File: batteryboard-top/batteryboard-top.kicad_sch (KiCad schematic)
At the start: 6 parts

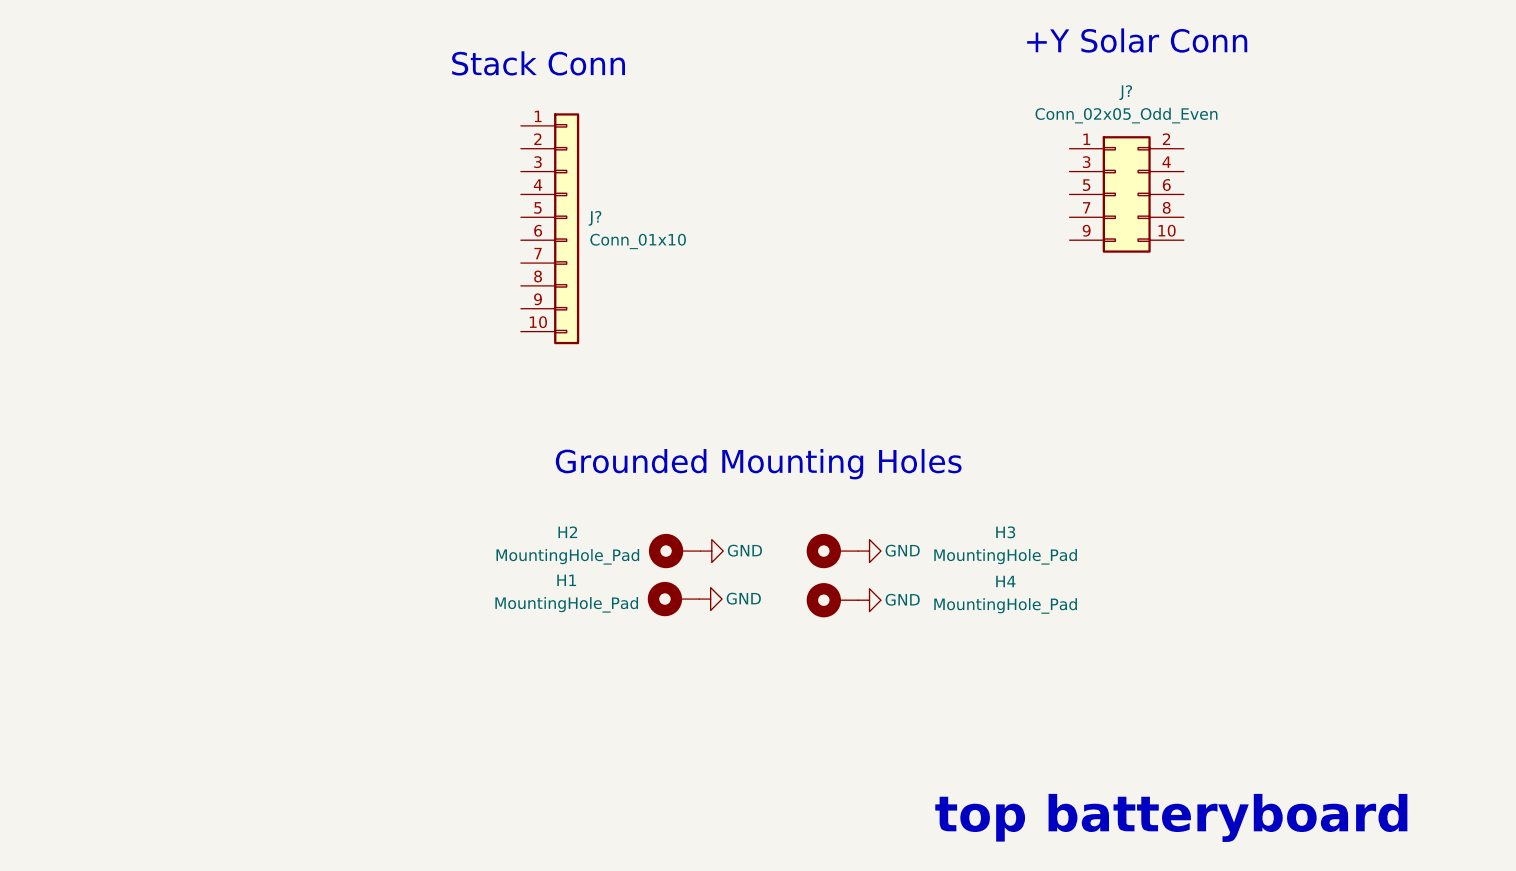
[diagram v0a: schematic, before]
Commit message: labeled connections
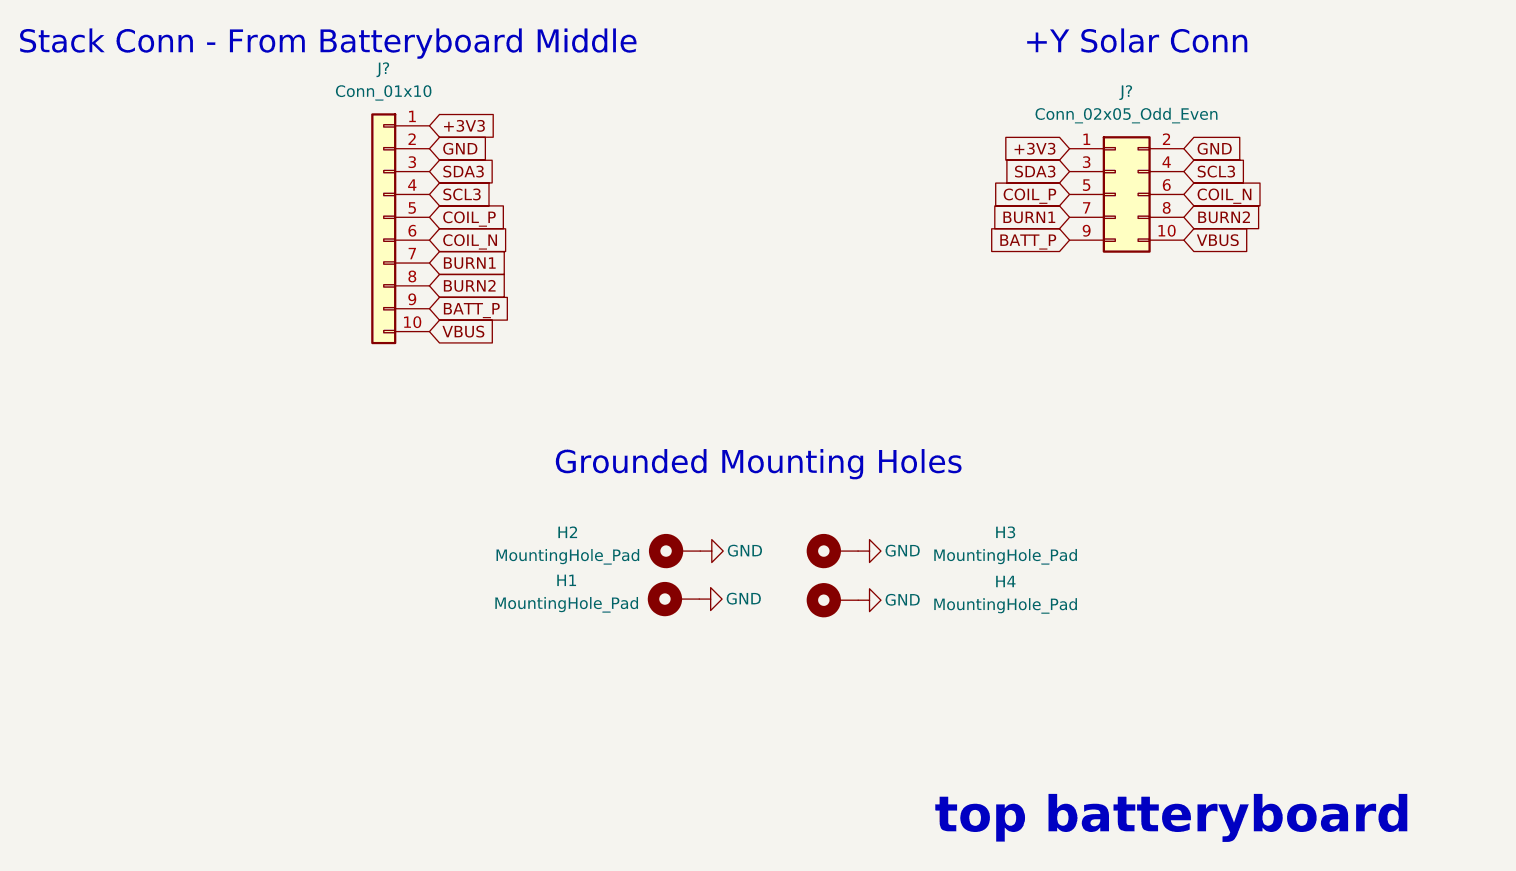
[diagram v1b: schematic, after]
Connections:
- net GND: now also J?.2 (Pin_2), J?.2 (Pin_2)
- net +3V3: now reaches J?.1 (Pin_1)
- net +3V3: now also J?.1 (Pin_1)
- net VBUS: now reaches J?.10 (Pin_10)
- net VBUS: now also J?.10 (Pin_10)
- net SDA3: now reaches J?.3 (Pin_3)
- net SDA3: now also J?.3 (Pin_3)
- net SCL3: now reaches J?.4 (Pin_4)
- net SCL3: now also J?.4 (Pin_4)
- net COIL_P: now reaches J?.5 (Pin_5)
- net COIL_P: now also J?.5 (Pin_5)
- net COIL_N: now reaches J?.6 (Pin_6)
- net COIL_N: now also J?.6 (Pin_6)
- net BURN1: now reaches J?.7 (Pin_7)
- net BURN1: now also J?.7 (Pin_7)
- net BURN2: now reaches J?.8 (Pin_8)
- net BURN2: now also J?.8 (Pin_8)
- net BATT_P: now reaches J?.9 (Pin_9)
- net BATT_P: now also J?.9 (Pin_9)
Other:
- note added: "Stack Conn - From Batteryboard Middle"
- note removed: "Stack Conn"
- moved on the sheet: J?
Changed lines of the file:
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@@
     (effects (font (size 2.54 2.54)) (justify left bottom))
   )
-  (text "Stack Conn" (at 70.866 30.48 0)
+  (text "Stack Conn - From Batteryboard Middle" (at 22.86 27.94 0)
     (effects (font (size 2.54 2.54)) (justify left bottom))
   )
@@
   (text "top batteryboard" (at 124.714 114.681 0)
     (effects (font (size 3.9878 3.9878) (thickness 1.016) bold) (justify left bottom))
+  )
+  (global_label "COIL_P" (shape input) (at 139.7 43.18 180) (fields_autoplaced)
+    (effects (font (size 1.27 1.27)) (justify right))
+    (property "Intersheet References" "${INTERSHEET_REFS}" (id 0) (at 130.8159 43.1006 0)
+      (effects (font (size 1.27 1.27)) (justify right) hide)
+    )
+  )
+  (global_label "COIL_P" (shape input) (at 68.58 45.72 0) (fields_autoplaced)
+    (effects (font (size 1.27 1.27)) (justify left))
+    (property "Intersheet References" "${INTERSHEET_REFS}" (id 0) (at 77.4641 45.6406 0)
+      (effects (font (size 1.27 1.27)) (justify left) hide)
+    )
+  )
+  (global_label "GND" (shape input) (at 152.4 38.1 0) (fields_autoplaced)
+    (effects (font (size 1.27 1.27)) (justify left))
+    (property "Intersheet References" "${INTERSHEET_REFS}" (id 0) (at 158.6836 38.0206 0)
+      (effects (font (size 1.27 1.27)) (justify left) hide)
+    )
+  )
+  (global_label "COIL_N" (shape input) (at 68.58 48.26 0) (fields_autoplaced)
+    (effects (font (size 1.27 1.27)) (justify left))
+    (property "Intersheet References" "${INTERSHEET_REFS}" (id 0) (at 77.5245 48.1806 0)
+      (effects (font (size 1.27 1.27)) (justify left) hide)
+    )
+  )
+  (global_label "VBUS" (shape input) (at 68.58 58.42 0) (fields_autoplaced)
+    (effects (font (size 1.27 1.27)) (justify left))
+    (property "Intersheet References" "${INTERSHEET_REFS}" (id 0) (at 75.8917 58.3406 0)
+      (effects (font (size 1.27 1.27)) (justify left) hide)
+    )
+  )
+  (global_label "SCL3" (shape input) (at 68.58 43.18 0) (fields_autoplaced)
+    (effects (font (size 1.27 1.27)) (justify left))
+    (property "Intersheet References" "${INTERSHEET_REFS}" (id 0) (at 75.7102 43.1006 0)
+      (effects (font (size 1.27 1.27)) (justify left) hide)
+    )
+  )
+  (global_label "VBUS" (shape input) (at 152.4 48.26 0) (fields_autoplaced)
+    (effects (font (size 1.27 1.27)) (justify left))
+    (property "Intersheet References" "${INTERSHEET_REFS}" (id 0) (at 159.7117 48.1806 0)
+      (effects (font (size 1.27 1.27)) (justify left) hide)
+    )
+  )
+  (global_label "BURN1" (shape input) (at 139.7 45.72 180) (fields_autoplaced)
+    (effects (font (size 1.27 1.27)) (justify right))
+    (property "Intersheet References" "${INTERSHEET_REFS}" (id 0) (at 130.8764 45.6406 0)
+      (effects (font (size 1.27 1.27)) (justify right) hide)
+    )
+  )
+  (global_label "BURN2" (shape input) (at 152.4 45.72 0) (fields_autoplaced)
+    (effects (font (size 1.27 1.27)) (justify left))
+    (property "Intersheet References" "${INTERSHEET_REFS}" (id 0) (at 161.2236 45.6406 0)
+      (effects (font (size 1.27 1.27)) (justify left) hide)
+    )
+  )
+  (global_label "SCL3" (shape input) (at 152.4 40.64 0) (fields_autoplaced)
+    (effects (font (size 1.27 1.27)) (justify left))
+    (property "Intersheet References" "${INTERSHEET_REFS}" (id 0) (at 159.5302 40.5606 0)
+      (effects (font (size 1.27 1.27)) (justify left) hide)
+    )
+  )
+  (global_label "COIL_N" (shape input) (at 152.4 43.18 0) (fields_autoplaced)
+    (effects (font (size 1.27 1.27)) (justify left))
+    (property "Intersheet References" "${INTERSHEET_REFS}" (id 0) (at 161.3445 43.1006 0)
+      (effects (font (size 1.27 1.27)) (justify left) hide)
+    )
+  )
+  (global_label "+3V3" (shape input) (at 68.58 35.56 0) (fields_autoplaced)
+    (effects (font (size 1.27 1.27)) (justify left))
+    (property "Intersheet References" "${INTERSHEET_REFS}" (id 0) (at 76.0731 35.4806 0)
+      (effects (font (size 1.27 1.27)) (justify left) hide)
+    )
+  )
+  (global_label "SDA3" (shape input) (at 68.58 40.64 0) (fields_autoplaced)
+    (effects (font (size 1.27 1.27)) (justify left))
+    (property "Intersheet References" "${INTERSHEET_REFS}" (id 0) (at 75.7707 40.5606 0)
+      (effects (font (size 1.27 1.27)) (justify left) hide)
+    )
+  )
+  (global_label "BATT_P" (shape input) (at 68.58 55.88 0) (fields_autoplaced)
+    (effects (font (size 1.27 1.27)) (justify left))
+    (property "Intersheet References" "${INTERSHEET_REFS}" (id 0) (at 77.5245 55.8006 0)
+      (effects (font (size 1.27 1.27)) (justify left) hide)
+    )
+  )
+  (global_label "+3V3" (shape input) (at 139.7 38.1 180) (fields_autoplaced)
+    (effects (font (size 1.27 1.27)) (justify right))
+    (property "Intersheet References" "${INTERSHEET_REFS}" (id 0) (at 132.2069 38.0206 0)
+      (effects (font (size 1.27 1.27)) (justify right) hide)
+    )
+  )
+  (global_label "SDA3" (shape input) (at 139.7 40.64 180) (fields_autoplaced)
+    (effects (font (size 1.27 1.27)) (justify right))
+    (property "Intersheet References" "${INTERSHEET_REFS}" (id 0) (at 132.5093 40.5606 0)
+      (effects (font (size 1.27 1.27)) (justify right) hide)
+    )
+  )
+  (global_label "GND" (shape input) (at 68.58 38.1 0) (fields_autoplaced)
+    (effects (font (size 1.27 1.27)) (justify left))
+    (property "Intersheet References" "${INTERSHEET_REFS}" (id 0) (at 74.8636 38.0206 0)
+      (effects (font (size 1.27 1.27)) (justify left) hide)
+    )
+  )
+  (global_label "BATT_P" (shape input) (at 139.7 48.26 180) (fields_autoplaced)
+    (effects (font (size 1.27 1.27)) (justify right))
+    (property "Intersheet References" "${INTERSHEET_REFS}" (id 0) (at 130.7555 48.1806 0)
+      (effects (font (size 1.27 1.27)) (justify right) hide)
+    )
+  )
+  (global_label "BURN2" (shape input) (at 68.58 53.34 0) (fields_autoplaced)
+    (effects (font (size 1.27 1.27)) (justify left))
+    (property "Intersheet References" "${INTERSHEET_REFS}" (id 0) (at 77.4036 53.2606 0)
+      (effects (font (size 1.27 1.27)) (justify left) hide)
+    )
+  )
+  (global_label "BURN1" (shape input) (at 68.58 50.8 0) (fields_autoplaced)
+    (effects (font (size 1.27 1.27)) (justify left))
+    (property "Intersheet References" "${INTERSHEET_REFS}" (id 0) (at 77.4036 50.7206 0)
+      (effects (font (size 1.27 1.27)) (justify left) hide)
+    )
   )
   (symbol (lib_id "power:GND") (at 98.552 88.138 90) (unit 1)
@@
     (pin "1")
   )
-  (symbol (lib_id "Connector_Generic:Conn_01x10") (at 83.82 45.72 0) (unit 1)
+  (symbol (lib_id "Connector_Generic:Conn_01x10") (at 63.5 45.72 0) (mirror y) (unit 1)
     (in_bom yes) (on_board yes) (fields_autoplaced)
-    (property "Reference" "J?" (id 0) (at 86.36 45.7199 0)
-      (effects (font (size 1.27 1.27)) (justify left))
-    )
-    (property "Value" "Conn_01x10" (id 1) (at 86.36 48.2599 0)
-      (effects (font (size 1.27 1.27)) (justify left))
-    )
-    (property "Footprint" "" (id 2) (at 83.82 45.72 0)
-      (effects (font (size 1.27 1.27)) hide)
-    )
-    (property "Datasheet" "~" (id 3) (at 83.82 45.72 0)
-      (effects (font (size 1.27 1.27)) hide)
-    )
+    (property "Reference" "J?" (id 0) (at 63.5 29.21 0))
+    (property "Value" "Conn_01x10" (id 1) (at 63.5 31.75 0))
+    (property "Footprint" "" (id 2) (at 63.5 45.72 0)
+      (effects (font (size 1.27 1.27)) hide)
+    )
+    (property "Datasheet" "~" (id 3) (at 63.5 45.72 0)
+      (effects (font (size 1.27 1.27)) hide)
+    )

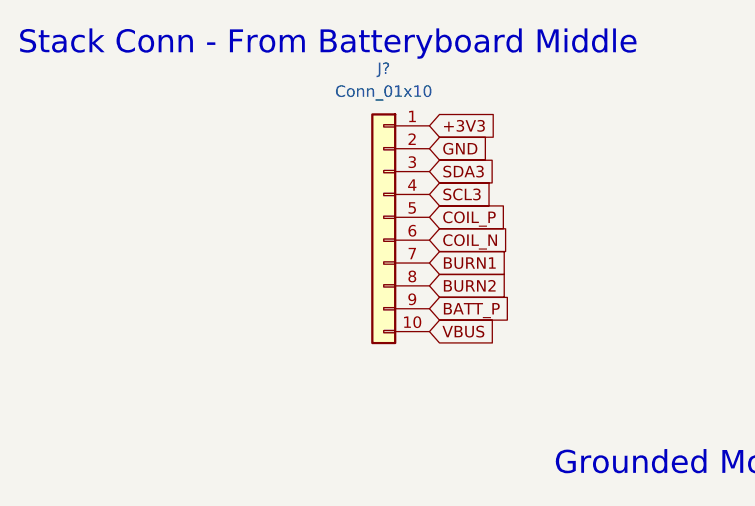
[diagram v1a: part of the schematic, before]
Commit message: switch to 2x connectors for battery boards
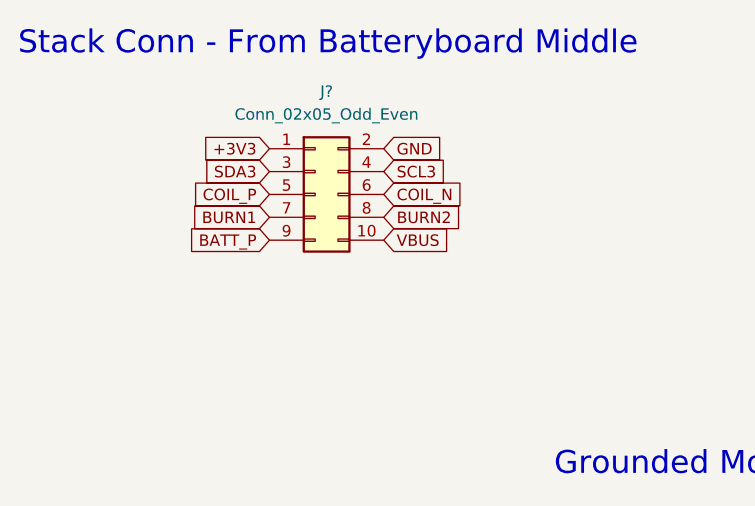
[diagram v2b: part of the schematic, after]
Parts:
- removed J?: Conn_01x10, symbol Connector_Generic:Conn_01x10
- added J?: Conn_02x05_Odd_Even, symbol Connector_Generic:Conn_02x05_Odd_Even
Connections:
- net +3V3: now also J?.1 (Pin_1)
- net BATT_P: now also J?.9 (Pin_9)
- net BURN1: now also J?.7 (Pin_7)
- net BURN2: now also J?.8 (Pin_8)
- net COIL_N: now also J?.6 (Pin_6)
- net COIL_P: now also J?.5 (Pin_5)
- net GND: now also J?.2 (Pin_2)
- net SCL3: now also J?.4 (Pin_4)
- net SDA3: now also J?.3 (Pin_3)
- net VBUS: now also J?.10 (Pin_10)
